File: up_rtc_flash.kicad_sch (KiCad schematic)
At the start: 14 parts, among them IC201 PCF8563T_5,518, IC202 W25Q128JVSIQTR, X201 PCIE-52P40H, X202 32.768 kHz, X203 TF-15×15, X204 CR1220-2ZX

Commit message: start rework of baseboard.
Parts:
- removed X201: PCIE-52P40H, eduboardv2:PCIE-SMD_PCIE-52P40H, symbol eduboardv2:PCIE-52P40H
- added J1: EduboardV2 PCIE UP Board Connector, EduboardV2_kicadlib:CONN-SMD_52P-P0.80-V_91304-70-052RXXX, symbol EduboardV2_kicadlib:EduboardUPConnector_GNDPads_V1
- renumbered C201 to C1, C202 to C2, C203 to C3, C204 to C4, D201 to D1, D202 to D2, IC201 to IC1, IC202 to IC2, R201 to R1, R202 to R2, X202 to X2, X203 to X3, X204 to X4

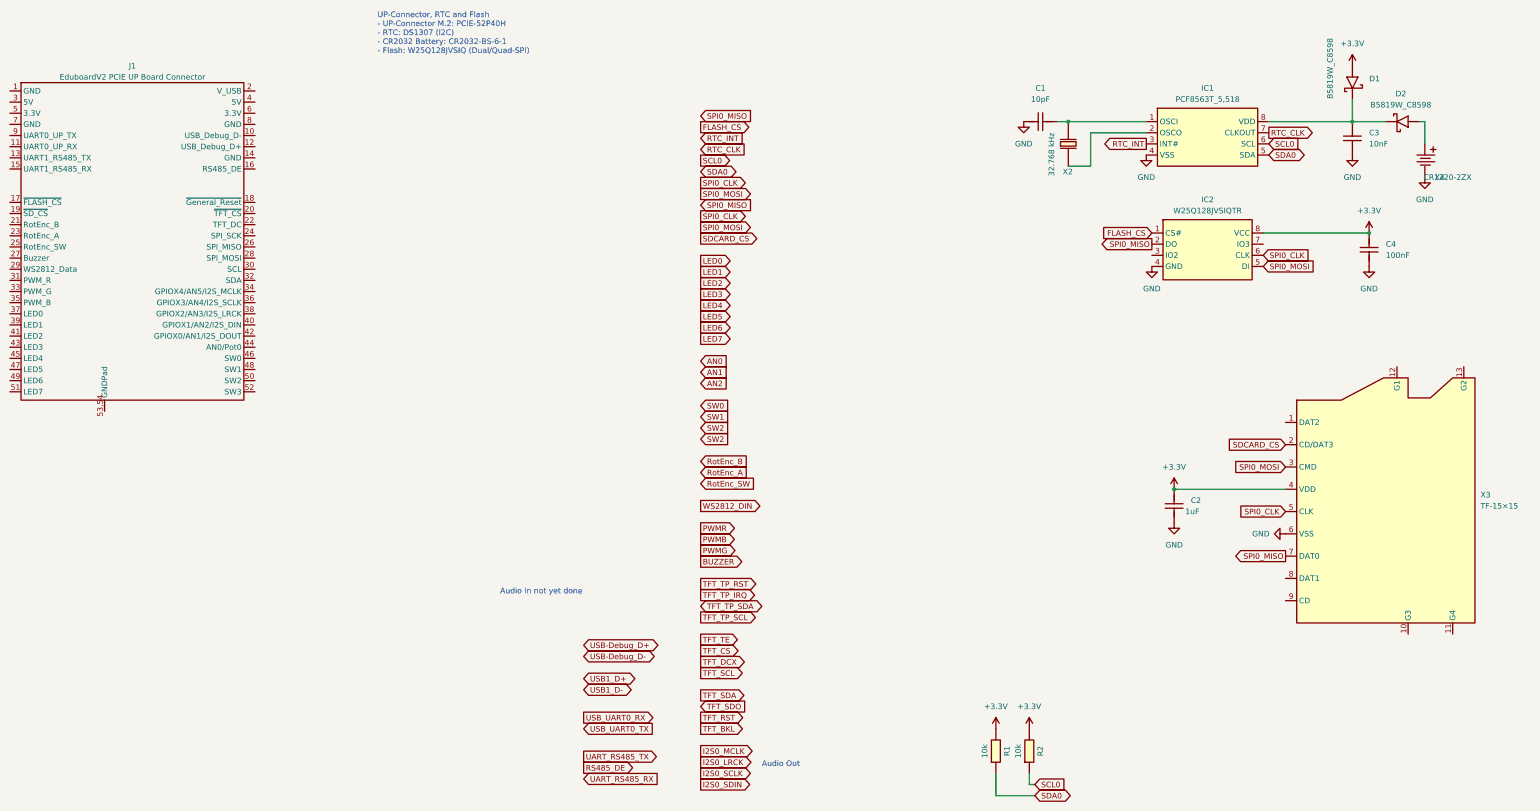
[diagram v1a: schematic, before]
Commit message: rework schematic. remove unnescessary stuff. Connect PCIE Connector. Select new Temperature Sensor (I2C) Define Signals for 40Pin Connector
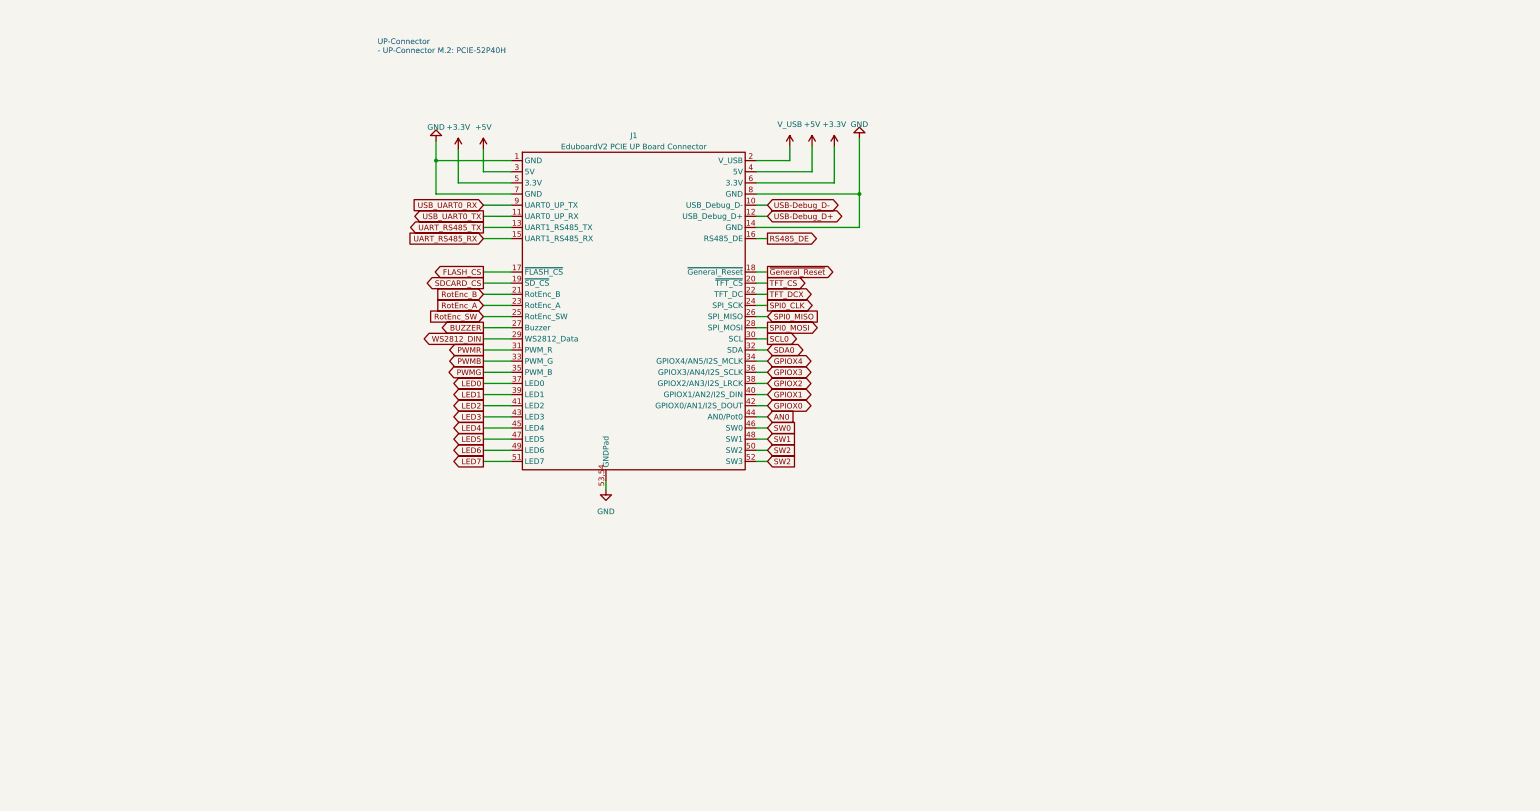
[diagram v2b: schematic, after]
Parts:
- removed C1: 10pF, eduboardv2:C0402, symbol eduboardv2:CL05C100JB5NNNC
- removed C2: 1uF, eduboardv2:C0402, symbol eduboardv2:CL05A105KA5NQNC
- removed C3: 10nF, eduboardv2:C0402, symbol eduboardv2:CL05B103KB5NNNC
- removed C4: 100nF, eduboardv2:C0402, symbol eduboardv2:CL05B104KB54PNC
- removed D1, D2: B5819W_C8598, eduboardv2:SOD-123_L2.7-W1.6-LS3.7-RD-1, symbol eduboardv2:B5819W_C8598
- removed IC1: PCF8563T_5,518, eduboardv2:SOIC-8_L5.0-W4.0-P1.27-LS6.0-BL, symbol eduboardv2:PCF8563T_5,518
- removed IC2: W25Q128JVSIQTR, eduboardv2:SOIC-8_L5.3-W5.3-P1.27-LS8.0-BL, symbol eduboardv2:W25Q128JVSIQTR
- removed R1, R2: 10k, eduboardv2:R0402, symbol eduboardv2:0402WGF100JTCE
- removed X2: 32.768 kHz, eduboardv2:FC-135R_L3.2-W1.5, symbol eduboardv2:Q13FC1350000400
- removed X3: TF-15×15, eduboardv2:TF-SMD_TF-15-15, symbol eduboardv2:TF-15×15
- removed X4: CR1220-2ZX, BAT-SMD_CR1220-2ZX, symbol eduboardv2:CR1220-2ZX
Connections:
- net +3.3V: now also J1.5 (3.3V), J1.6 (3.3V)
- net AN0: now also J1.44 (AN0/Pot0)
- net BUZZER: now also J1.27 (Buzzer)
- net FLASH_CS: now also J1.17 (~{FLASH_CS})
- net GND: now also J1.1 (GND), J1.14 (GND), J1.53,54 (GNDPad), J1.7 (GND), J1.8 (GND)
- net LED0: now also J1.37 (LED0)
- net LED1: now also J1.39 (LED1)
- net LED2: now also J1.41 (LED2)
- net LED3: now also J1.43 (LED3)
- net LED4: now also J1.45 (LED4)
- net LED5: now also J1.47 (LED5)
- net LED6: now also J1.49 (LED6)
- net LED7: now also J1.51 (LED7)
- net PWMB: now also J1.33 (PWM_G)
- net PWMG: now also J1.35 (PWM_B)
- net PWMR: now also J1.31 (PWM_R)
- net RS485_DE: now also J1.16 (RS485_DE)
- net RotEnc_A: now also J1.23 (RotEnc_A)
- net RotEnc_B: now also J1.21 (RotEnc_B)
- net RotEnc_SW: now also J1.25 (RotEnc_SW)
- net SCL0: now also J1.30 (SCL)
- net SDA0: now also J1.32 (SDA)
- net SDCARD_CS: now also J1.19 (~{SD_CS})
- net SPI0_CLK: now also J1.24 (SPI_SCK)
- net SPI0_MISO: now also J1.26 (SPI_MISO)
- net SPI0_MOSI: now also J1.28 (SPI_MOSI)
- net SW0: now also J1.46 (SW0)
- net SW1: now also J1.48 (SW1)
- net SW2: now also J1.50 (SW2), J1.52 (SW3)
- net TFT_CS: now also J1.20 (~{TFT_CS})
- net TFT_DCX: now also J1.22 (TFT_DC)
- net UART_RS485_RX: now also J1.15 (UART1_RS485_RX)
- net UART_RS485_TX: now also J1.13 (UART1_RS485_TX)
- net USB-Debug_D+: now also J1.12 (USB_Debug_D+)
- net USB-Debug_D-: now also J1.10 (USB_Debug_D-)
- net USB_UART0_RX: now also J1.9 (UART0_UP_TX)
- net USB_UART0_TX: now also J1.11 (UART0_UP_RX)
- net WS2812_DIN: now also J1.29 (WS2812_Data)
- net ~{General_Reset}: now reaches J1.18 (~{General_Reset})
- net V_USB: now reaches J1.2 (V_USB)
- net +5V: now reaches J1.3 (5V)
- net +5V: now also J1.4 (5V)
- net GPIOX4: now reaches J1.34 (GPIOX4/AN5/I2S_MCLK)
- net GPIOX3: now reaches J1.36 (GPIOX3/AN4/I2S_SCLK)
- net GPIOX2: now reaches J1.38 (GPIOX2/AN3/I2S_LRCK)
- net GPIOX1: now reaches J1.40 (GPIOX1/AN2/I2S_DIN)
- net GPIOX0: now reaches J1.42 (GPIOX0/AN1/I2S_DOUT)
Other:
- note added: "UP-Connector - UP-Connector M.2: PCIE-52P40H"
- note removed: "Audio In not yet done"
- note removed: "Audio Out"
- note removed: "UP-Connector, RTC and Flash - UP-Connector M.2: PCIE-52P40H - RTC: DS1307 (I2C) - CR2032 Battery: CR2032-BS-6-1 - Flash: W25Q128JVSIQ (Dual/Quad-SPI)"
- moved on the sheet: J1

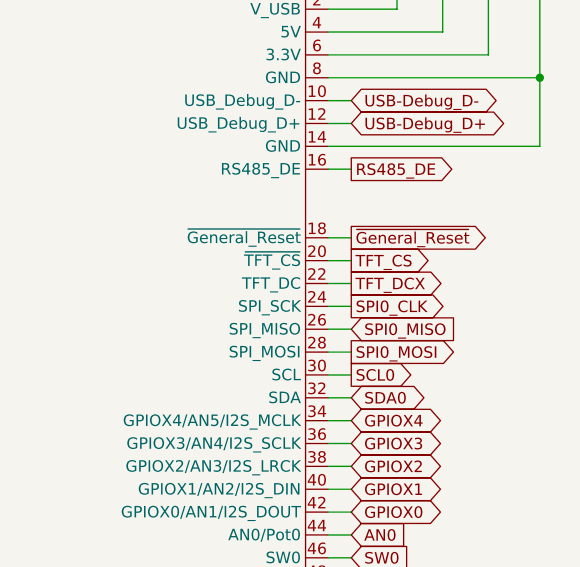
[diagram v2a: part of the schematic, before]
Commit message: replace display with better module, start layout parts on pcb.
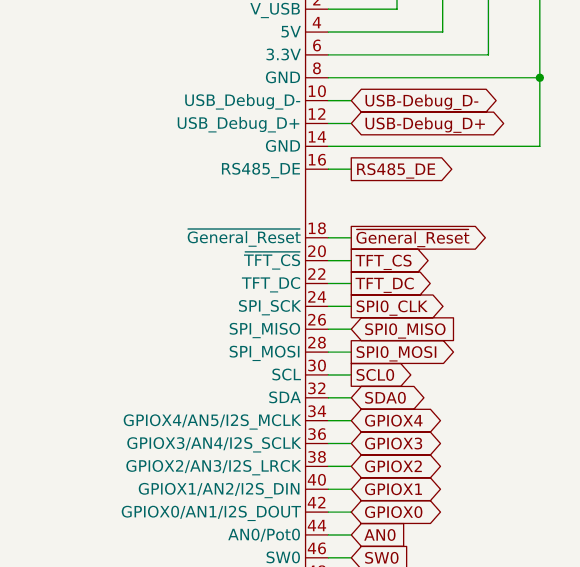
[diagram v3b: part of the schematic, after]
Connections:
- net TFT_DCX renamed TFT_DC
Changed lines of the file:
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@@
     )
   )
-  (global_label "TFT_DCX" (shape output) (at 102.87 78.74 0) (fields_autoplaced)
+  (global_label "TFT_DC" (shape output) (at 102.87 78.74 0) (fields_autoplaced)
     (effects (font (size 1.27 1.27)) (justify left))
-    (property "Intersheetrefs" "${INTERSHEET_REFS}" (at 113.0241 78.8194 0)
+    (property "Intersheetrefs" "${INTERSHEET_REFS}" (at 112.3072 78.74 0)
       (effects (font (size 1.27 1.27)) (justify left) hide)
     )

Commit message: Layout of parts done. Started laying tracks
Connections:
- net GND: now also J1.53 (GNDPad), J1.54 (GNDPad); no longer J1.53,54 (GNDPad)
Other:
- moved on the sheet: J1
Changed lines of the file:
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@@
     (pin "51")
     (pin "52")
-    (pin "53,54")
+    (pin "53")
+    (pin "54")
     (pin "6")
     (pin "7")

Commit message: proceed with layout
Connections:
- net SW2: no longer J1.52 (SW3)
- new net SW3: J1.52 (SW3)
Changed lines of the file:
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@@
     )
   )
-  (global_label "SW2" (shape input) (at 102.87 116.84 0) (fields_autoplaced)
+  (global_label "SW3" (shape input) (at 102.87 116.84 0) (fields_autoplaced)
     (effects (font (size 1.27 1.27)) (justify left))
-    (property "Intersheetrefs" "${INTERSHEET_REFS}" (at 109.1536 116.7606 0)
+    (property "Intersheetrefs" "${INTERSHEET_REFS}" (at 109.6462 116.84 0)
       (effects (font (size 1.27 1.27)) (justify left) hide)
     )

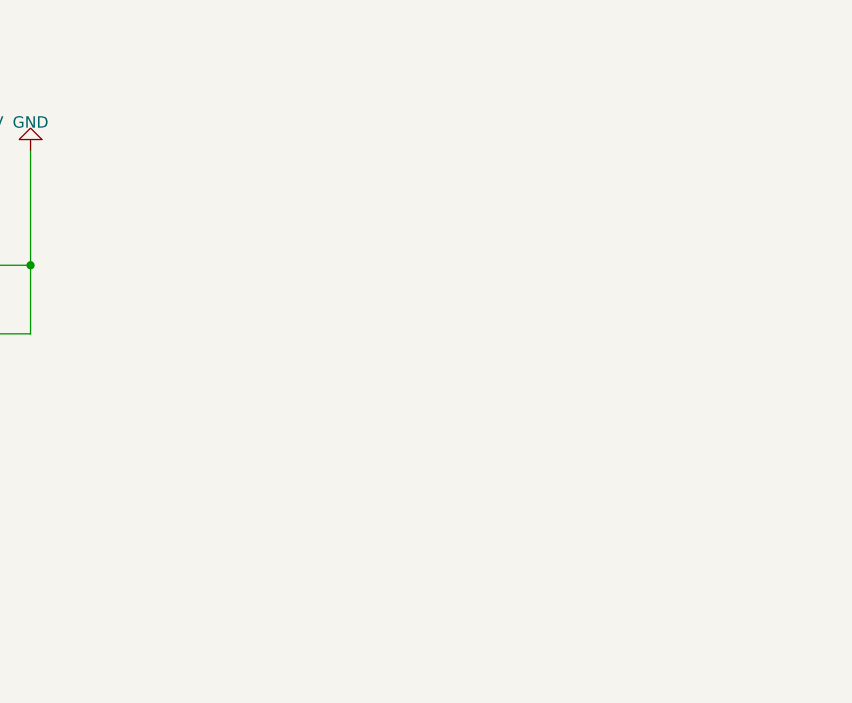
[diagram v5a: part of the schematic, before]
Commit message: add pullup resistors to cs pins and change dac pins to gpiox0 and 1 (AN0 is connected to pot)
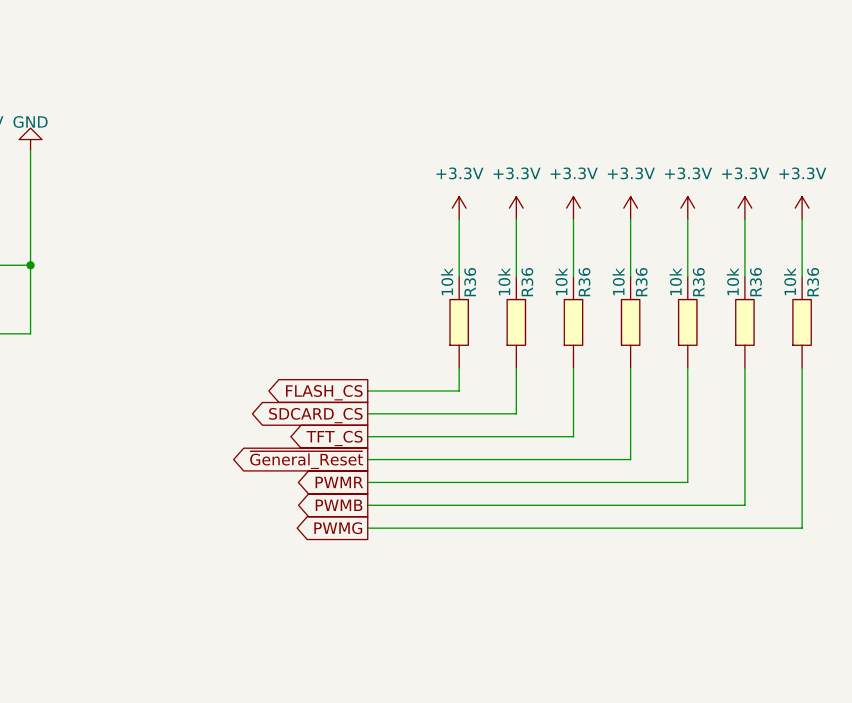
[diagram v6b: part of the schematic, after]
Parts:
- added R36 (x7): 10k, Resistor_SMD:R_0402_1005Metric_Pad0.72x0.64mm_HandSolder, symbol eduboardv2:0402WGF100JTCE
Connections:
- net +3.3V: now also R36.2, R36.2, R36.2, R36.2, R36.2, R36.2, R36.2
- net FLASH_CS: now also R36.1
- net PWMB: now also R36.1
- net PWMG: now also R36.1
- net PWMR: now also R36.1
- net SDCARD_CS: now also R36.1
- net TFT_CS: now also R36.1
- net ~{General_Reset}: now also R36.1

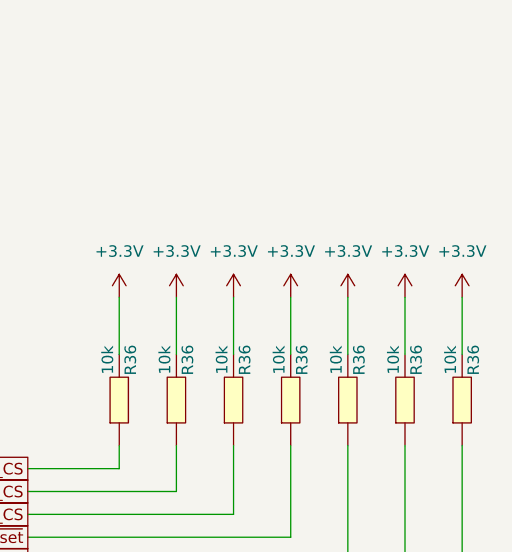
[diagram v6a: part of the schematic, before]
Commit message: set pwm channels to pull down
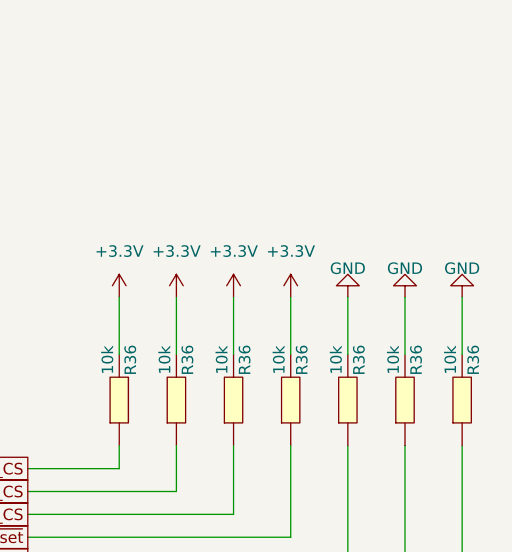
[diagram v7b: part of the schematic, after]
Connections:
- net +3.3V: no longer R36.2, R36.2, R36.2
- net GND: now also R36.2, R36.2, R36.2
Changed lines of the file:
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@@
-    )
-  )
-  (symbol (lib_id "eduboardv2:+3.3V") (at 203.2 50.8 0) (unit 1)
-    (in_bom yes) (on_board yes) (dnp no) (fields_autoplaced)
-    (property "Reference" "#PWR0211" (at 203.2 54.61 0)
-      (effects (font (size 1.27 1.27)) hide)
-    )
-    (property "Value" "+3.3V" (at 203.2 45.72 0)
-      (effects (font (size 1.27 1.27)))
-    )
-    (property "Footprint" "" (at 203.2 50.8 0)
-      (effects (font (size 1.27 1.27)) hide)
-    )
-    (property "Datasheet" "" (at 203.2 50.8 0)
-      (effects (font (size 1.27 1.27)) hide)
-    )
-    (pin "1")
-    (instances
-      (project "EduboardV2_Baseboard"
-        (path "/280adf03-05ea-4001-ab24-a5a43e6d4cc9/dc18459b-bf67-402d-bc74-ca4debdbcff4"
-          (reference "#PWR0211") (unit 1)
-        )
-      )
     )
   )
@@
     )
   )
-  (symbol (lib_id "eduboardv2:+3.3V") (at 196.85 50.8 0) (unit 1)
-    (in_bom yes) (on_board yes) (dnp no) (fields_autoplaced)
-    (property "Reference" "#PWR0210" (at 196.85 54.61 0)
-      (effects (font (size 1.27 1.27)) hide)
-    )
-    (property "Value" "+3.3V" (at 196.85 45.72 0)
-      (effects (font (size 1.27 1.27)))
-    )
-    (property "Footprint" "" (at 196.85 50.8 0)
-      (effects (font (size 1.27 1.27)) hide)
-    )
-    (property "Datasheet" "" (at 196.85 50.8 0)
-      (effects (font (size 1.27 1.27)) hide)
-    )
-    (pin "1")
-    (instances
-      (project "EduboardV2_Baseboard"
-        (path "/280adf03-05ea-4001-ab24-a5a43e6d4cc9/dc18459b-bf67-402d-bc74-ca4debdbcff4"
-          (reference "#PWR0210") (unit 1)
+  (symbol (lib_id "eduboardv2:GND") (at 203.2 50.8 180) (unit 1)
+    (in_bom yes) (on_board yes) (dnp no) (fields_autoplaced)
+    (property "Reference" "#PWR0211" (at 203.2 44.45 0)
+      (effects (font (size 1.27 1.27)) hide)
+    )
+    (property "Value" "GND" (at 203.2 47.625 0)
+      (effects (font (size 1.27 1.27)))
+    )
+    (property "Footprint" "" (at 203.2 50.8 0)
+      (effects (font (size 1.27 1.27)) hide)
+    )
+    (property "Datasheet" "" (at 203.2 50.8 0)
+      (effects (font (size 1.27 1.27)) hide)
+    )
+    (pin "1")
+    (instances
+      (project "EduboardV2_Baseboard"
+        (path "/280adf03-05ea-4001-ab24-a5a43e6d4cc9/dc18459b-bf67-402d-bc74-ca4debdbcff4"
+          (reference "#PWR0211") (unit 1)
         )
       )
@@
     )
   )
-  (symbol (lib_id "eduboardv2:+3.3V") (at 209.55 50.8 0) (unit 1)
-    (in_bom yes) (on_board yes) (dnp no) (fields_autoplaced)
-    (property "Reference" "#PWR0212" (at 209.55 54.61 0)
-      (effects (font (size 1.27 1.27)) hide)
-    )
-    (property "Value" "+3.3V" (at 209.55 45.72 0)
+  (symbol (lib_id "eduboardv2:GND") (at 196.85 50.8 180) (unit 1)
+    (in_bom yes) (on_board yes) (dnp no) (fields_autoplaced)
+    (property "Reference" "#PWR0210" (at 196.85 44.45 0)
+      (effects (font (size 1.27 1.27)) hide)
+    )
+    (property "Value" "GND" (at 196.85 47.625 0)
+      (effects (font (size 1.27 1.27)))
+    )
+    (property "Footprint" "" (at 196.85 50.8 0)
+      (effects (font (size 1.27 1.27)) hide)
+    )
+    (property "Datasheet" "" (at 196.85 50.8 0)
+      (effects (font (size 1.27 1.27)) hide)
+    )
+    (pin "1")
+    (instances
+      (project "EduboardV2_Baseboard"
+        (path "/280adf03-05ea-4001-ab24-a5a43e6d4cc9/dc18459b-bf67-402d-bc74-ca4debdbcff4"
+          (reference "#PWR0210") (unit 1)
+        )
+      )
+    )
+  )
+  (symbol (lib_id "eduboardv2:+3.3V") (at 118.11 45.085 0) (unit 1)
+    (in_bom yes) (on_board yes) (dnp no) (fields_autoplaced)
+    (property "Reference" "#PWR0117" (at 118.11 48.895 0)
+      (effects (font (size 1.27 1.27)) hide)
+    )
+    (property "Value" "+3.3V" (at 118.11 40.005 0)
+      (effects (font (size 1.27 1.27)))
+    )
+    (property "Footprint" "" (at 118.11 45.085 0)
+      (effects (font (size 1.27 1.27)) hide)
+    )
+    (property "Datasheet" "" (at 118.11 45.085 0)
+      (effects (font (size 1.27 1.27)) hide)
+    )
+    (pin "1")
+    (instances
+      (project "EduboardV2_Baseboard"
+        (path "/280adf03-05ea-4001-ab24-a5a43e6d4cc9/dc18459b-bf67-402d-bc74-ca4debdbcff4"
+          (reference "#PWR0117") (unit 1)
+        )
+      )
+    )
+  )
+  (symbol (lib_id "eduboardv2:GND") (at 209.55 50.8 180) (unit 1)
+    (in_bom yes) (on_board yes) (dnp no) (fields_autoplaced)
+    (property "Reference" "#PWR0212" (at 209.55 44.45 0)
+      (effects (font (size 1.27 1.27)) hide)
+    )
+    (property "Value" "GND" (at 209.55 47.625 0)
       (effects (font (size 1.27 1.27)))
     )
@@
         )
       )
-    )
-  )
-  (symbol (lib_id "eduboardv2:+3.3V") (at 118.11 45.085 0) (unit 1)
-    (in_bom yes) (on_board yes) (dnp no) (fields_autoplaced)
-    (property "Reference" "#PWR0117" (at 118.11 48.895 0)
-      (effects (font (size 1.27 1.27)) hide)
-    )
-    (property "Value" "+3.3V" (at 118.11 40.005 0)
-      (effects (font (size 1.27 1.27)))
-    )
-    (property "Footprint" "" (at 118.11 45.085 0)
-      (effects (font (size 1.27 1.27)) hide)
-    )
-    (property "Datasheet" "" (at 118.11 45.085 0)
-      (effects (font (size 1.27 1.27)) hide)
-    )
-    (pin "1")
-    (instances
-      (project "EduboardV2_Baseboard"
-        (path "/280adf03-05ea-4001-ab24-a5a43e6d4cc9/dc18459b-bf67-402d-bc74-ca4debdbcff4"
-          (reference "#PWR0117") (unit 1)
-        )
-      )
